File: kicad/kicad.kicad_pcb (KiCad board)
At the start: 4 copper layers, 135 parts, among them Q1 PMF170XP,115, Q2 FS8205A_C2830320, SW1 TS-1088-AR02016, U1 74AHC1G14GW,125, U2 E73-2G4M08S1C, U3 BL8573CS8TR, U4 DW01A, U5 S2B-PH-K-S(LF)(SN), U6 LP5024RSMR, U7 SN74HCS74BQAR, X3 FC-13532.768KHZ9PF20PPM

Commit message: psb outline
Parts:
- removed hex_outline (x36): , clipboard:b9cf7df6-7b49-4194-bf11-16aaca528749
- added hex_edge: , clipboard:b9cf7df6-7b49-4194-bf11-16aaca528749, F.Cu at (104.2, 49.4)
- added hex_edge: , clipboard:b9cf7df6-7b49-4194-bf11-16aaca528749, F.Cu at (215.9, 92.4)
- added hex_edge: , clipboard:b9cf7df6-7b49-4194-bf11-16aaca528749, F.Cu at (215.9, 70.9)
- added hex_edge: , clipboard:b9cf7df6-7b49-4194-bf11-16aaca528749, F.Cu at (178.6, 71.0)
- added hex_edge: , clipboard:b9cf7df6-7b49-4194-bf11-16aaca528749, F.Cu at (215.9, 49.4)
- added hex_edge: , clipboard:b9cf7df6-7b49-4194-bf11-16aaca528749, F.Cu at (104.2, 70.9)
- added hex_edge: , clipboard:b9cf7df6-7b49-4194-bf11-16aaca528749, F.Cu at (197.2, 38.7)
- added hex_edge: , clipboard:b9cf7df6-7b49-4194-bf11-16aaca528749, F.Cu at (122.9, 38.7)
- added hex_edge: , clipboard:b9cf7df6-7b49-4194-bf11-16aaca528749, F.Cu at (122.8, 103.2)
- added hex_edge: , hexcaps:PG1350_hotswap, B.Cu at (160.0, 103.2)
- added hex_edge: , clipboard:b9cf7df6-7b49-4194-bf11-16aaca528749, F.Cu at (141.4, 49.4)
- added hex_edge: , clipboard:b9cf7df6-7b49-4194-bf11-16aaca528749, F.Cu at (178.6, 27.9)
- added hex_edge: , clipboard:b9cf7df6-7b49-4194-bf11-16aaca528749, F.Cu at (160.0, 38.7)
- added hex_edge: , clipboard:b9cf7df6-7b49-4194-bf11-16aaca528749, F.Cu at (104.2, 113.9)
- added hex_edge: , clipboard:b9cf7df6-7b49-4194-bf11-16aaca528749, F.Cu at (160.1, 81.7)
- added hex_edge: , clipboard:b9cf7df6-7b49-4194-bf11-16aaca528749, F.Cu at (197.2, 81.7)
- added hex_edge: , clipboard:b9cf7df6-7b49-4194-bf11-16aaca528749, F.Cu at (104.1, 92.4)
- added hex_edge: , clipboard:b9cf7df6-7b49-4194-bf11-16aaca528749, F.Cu at (141.4, 113.9)
- added key_template (x2): , hexcaps:PG1350_hotswap, B.Cu at (104.2, 92.4)
- added key_template: , hexcaps:PG1350_hotswap, B.Cu at (122.8, 81.7)
- added key_template (x2): , hexcaps:PG1350_hotswap, B.Cu at (104.2, 70.9)
- added key_template: , hexcaps:PG1350_hotswap, B.Cu at (270.7, 45.8)
- Battery?, Q2, R10, R8, R9, U3, U4, U5: moved to B.Cu
- moved C25 38.0 mm to (124.9, 84.2)
- moved R11 38.0 mm to (124.9, 82.9)
- moved R12 38.0 mm to (124.9, 79.2)
- moved R13 38.0 mm to (124.9, 80.4)
- moved R14 38.0 mm to (124.9, 81.7)
- moved U6 38.0 mm to (129.1, 81.1)
- moved C26 38.0 mm to (124.8, 77.8)
- moved U5 35.9 mm to (113.3, 39.7), turned to 0 degrees
- moved U4 34.1 mm to (127.2, 45.3)
- moved Q2 34.0 mm to (127.2, 41.0)
- moved D2 31.5 mm to (100.1, 63.3), turned to 0 degrees
- moved D1 30.4 mm to (102.2, 63.3), turned to 180 degrees
- moved R4 29.9 mm to (100.1, 64.5), turned to 0 degrees
- moved D3 28.8 mm to (102.2, 64.5), turned to 180 degrees
- moved C3 28.3 mm to (100.2, 65.8), turned to 180 degrees
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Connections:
- U6 pad 1: /LED20 -> /LED16
- U6 pad 10: /LED7 -> unconnected-(U6-OUT9-Pad10)
- U6 pad 11: /LED6 -> /LED2
- U6 pad 12: /LED10 -> /LED6
- U6 pad 13: /LED11 -> /LED10
- U6 pad 14: /LED15 -> /LED14
- U6 pad 15: /LED14 -> unconnected-(U6-OUT14-Pad15)
- U6 pad 16: /LED18 -> unconnected-(U6-OUT15-Pad16)
- U6 pad 17: /LED19 -> /LED18
- U6 pad 18: /LED8 -> /LED1
- U6 pad 19: /LED12 -> /LED5
- U6 pad 2: /LED4 -> /LED12
- U6 pad 20: /LED16 -> /LED9
- U6 pad 21: unconnected-(U6-OUT20-Pad21) -> /LED13
- U6 pad 22: unconnected-(U6-OUT21-Pad22) -> /LED17
- U6 pad 23: unconnected-(U6-OUT22-Pad23) -> /LED4
- U6 pad 24: unconnected-(U6-OUT23-Pad24) -> /LED20
- U6 pad 3: /LED17 -> /LED8
- U6 pad 4: /LED13 -> /LED19
- U6 pad 5: /LED9 -> /LED15
- U6 pad 6: /LED5 -> /LED11
- U6 pad 7: /LED1 -> /LED7
- U6 pad 8: /LED2 -> /LED3
- U6 pad 9: /LED3 -> unconnected-(U6-OUT8-Pad9)
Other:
- board outline added: 127.3 x 89.6 mm

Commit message: .
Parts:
- removed D1, D2: NSR05F20NXT5G, easyeda2kicad:DSN2_L1.0-W0.6-RD
- added R15: RC0402FR-074M3L, easyeda2kicad:R0402, F.Cu at (84.2, 65.0)
- added R16: RC0402FR-071ML, easyeda2kicad:R0402, F.Cu at (84.2, 67.1)
- U1: value 74AHC1G14GW,125 -> TLV7031QDCKRQ1; footprint easyeda2kicad:SOT-353_L2.1-W1.3-P0.65-LS2.3-BR -> easyeda2kicad:SC-70-5_L2.0-W1.3-P0.65-LS2.1-BR
- moved R1 18.9 mm to (84.2, 60.7)
- moved D3 18.6 mm to (84.2, 69.2), turned to 0 degrees
- moved Q1 16.3 mm to (87.5, 65.2), turned to 0 degrees
- moved R4 16.0 mm to (84.2, 62.8)
- moved U1 14.4 mm to (87.7, 68.5), turned to 0 degrees
- moved U7 13.0 mm to (88.4, 61.5), turned to 0 degrees
- moved C3 9.37 mm to (90.9, 64.6), turned to 0 degrees
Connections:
- C3 pad 1: Net-(U1-A) -> Net-(U1-IN+)
- D3 pad 1: Net-(D1-Pad1) -> /PWR_BTN
- D3 pad 2: Net-(U1-A) -> Net-(U1-IN+)
- R1 pad 1: Net-(D1-Pad1) -> /PWR_BTN
- R4 pad 1: Net-(D2-Pad1) -> /PWR_BTN
- R4 pad 2: Net-(U1-A) -> Net-(U1-IN+)
- U1 pad 1: unconnected-(U1-NC-Pad1) -> Net-(U1-OUT)
- U1 pad 2: Net-(U1-A) -> GND
- U1 pad 3: GND -> Net-(U1-IN+)
- U1 pad 4: Net-(U1-Y) -> Net-(U1-IN-)
- U1 pad 5: /BAT+ -> /PWR_BTN
- U7 pad 3: Net-(U1-Y) -> Net-(U1-OUT)

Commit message: ..
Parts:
- added component_safe_space: , hexcaps:PG1350_hotswap, B.Cu at (104.1, 92.4)
- added component_safe_space: , hexcaps:PG1350_hotswap, B.Cu at (104.2, 70.9)
- added component_safe_space: , hexcaps:PG1350_hotswap, B.Cu at (122.8, 81.7)
- moved C3 12.2 mm to (102.3, 68.9)
- moved D3 12.2 mm to (95.7, 73.6)
- moved Q1 12.2 mm to (99.0, 69.5)
- moved R16 12.2 mm to (95.6, 71.4)
- moved R4 12.2 mm to (95.6, 67.1)
- moved R1 12.2 mm to (95.6, 65.0)
- moved U7 12.2 mm to (99.9, 65.8)
- moved R15 12.2 mm to (95.6, 69.3)
- moved U1 12.2 mm to (99.2, 72.8)
- moved C25 2.72 mm to (122.2, 84.9)
- moved C26 2.72 mm to (122.2, 78.6)
- moved R11 2.72 mm to (122.2, 83.7)
- moved R12 2.72 mm to (122.2, 79.9)
- moved R13 2.72 mm to (122.2, 81.2)
- moved R14 2.72 mm to (122.2, 82.4)
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- renumbered key_template to component_case_outline

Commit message: ...
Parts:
- added C10: GRM033C71C104KE14D, easyeda2kicad:C0201, F.Cu at (98.3, 29.6)
- added C11: GRM033C71C104KE14D, easyeda2kicad:C0201, F.Cu at (99.3, 31.2)
- added C12: GRM033C71C104KE14D, easyeda2kicad:C0201, F.Cu at (100.3, 32.9)
- added C13: GRM033C71C104KE14D, easyeda2kicad:C0201, F.Cu at (98.6, 24.9)
- added C14: GRM033C71C104KE14D, easyeda2kicad:C0201, F.Cu at (99.6, 26.6)
- added C15: GRM033C71C104KE14D, easyeda2kicad:C0201, F.Cu at (100.5, 28.3)
- added C16: GRM033C71C104KE14D, easyeda2kicad:C0201, F.Cu at (101.5, 30.0)
- added C17: GRM033C71C104KE14D, easyeda2kicad:C0201, F.Cu at (102.5, 31.6)
- added C18: GRM033C71C104KE14D, easyeda2kicad:C0201, F.Cu at (100.8, 23.7)
- added C19: GRM033C71C104KE14D, easyeda2kicad:C0201, F.Cu at (101.8, 25.4)
- added C20: GRM033C71C104KE14D, easyeda2kicad:C0201, F.Cu at (102.7, 27.0)
- added C21: GRM033C71C104KE14D, easyeda2kicad:C0201, F.Cu at (103.7, 28.7)
- added C22: GRM033C71C104KE14D, easyeda2kicad:C0201, F.Cu at (104.7, 30.4)
- added C23: GRM033C71C104KE14D, easyeda2kicad:C0201, F.Cu at (103.0, 22.4)
- added C24: GRM033C71C104KE14D, easyeda2kicad:C0201, F.Cu at (104.0, 24.1)
- added C25: GRM033C71C104KE14D, easyeda2kicad:C0201, F.Cu at (104.9, 25.8)
- added C26: GRM033C71C104KE14D, easyeda2kicad:C0201, F.Cu at (105.9, 27.4)
- added C27: GRM033C71C104KE14D, easyeda2kicad:C0201, F.Cu at (106.8, 29.1)
- added C8: GRM033C71C104KE14D, easyeda2kicad:C0201, F.Cu at (96.4, 26.2)
- added C9: GRM033C71C104KE14D, easyeda2kicad:C0201, F.Cu at (97.4, 27.9)
- turned R8 to 180 degrees
- renumbered C3 to C1, C11 to C2, C27 to C3, C28 to C4, C29 to C5, C25 to C6, C26 to C7, D3 to D1, D13 to D10, D17 to D11, D21 to D12, D15 to D13, D6 to D14, D10 to D15, D14 to D16, D18 to D17, D22 to D18, D11 to D19, D4 to D2, D19 to D20, D8 to D3, D12 to D4, D16 to D5, D20 to D6, D5 to D8, LED17 to LED10, LED4 to LED11, LED14 to LED12, LED11 to LED13, LED8 to LED14, LED18 to LED15, LED15 to LED16, LED12 to LED17, LED19 to LED18, LED16 to LED19, LED5 to LED2, LED2 to LED3, LED9 to LED4, LED6 to LED5, LED3 to LED6, LED13 to LED7, LED10 to LED8, LED7 to LED9, R4 to R1, R5 to R10, R2 to R11, R3 to R12, R11 to R13, R12 to R14, R13 to R15, R14 to R16, R6 to R2, R8 to R3, R9 to R4, R10 to R5, R1 to R6, R15 to R8, R16 to R9, S14 to S11, S18 to S12, S12 to S13, S3 to S14, S7 to S15, S11 to S16, S15 to S17, S19 to S18, S8 to S19, S5 to S2, S16 to S20, S9 to S3, S13 to S4, S17 to S5, S4 to S6, S20 to S7, S2 to S8, S6 to S9, U4 to U1, U3 to U2, U1 to U3, U7 to U4, U2 to U6, U6 to U7, X3 to X1

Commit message: ... started doing wiring
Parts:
- C1, C10, D1, Q1: moved to B.Cu
- C11: renamed from C20; moved to B.Cu
- C12: renamed from C11; moved to B.Cu
- C13: renamed from C21; moved to B.Cu
- C14: renamed from C12; moved to B.Cu
- C15: renamed from C22; moved to B.Cu
- C16: renamed from C13; moved to B.Cu
- C17: renamed from C23; moved to B.Cu
- C18: renamed from C14; moved to B.Cu
- C19: renamed from C24; moved to B.Cu
- C20: renamed from C15; moved to B.Cu
- C21: renamed from C25; moved to B.Cu
- C22: renamed from C16; moved to B.Cu
- C23: renamed from C26; moved to B.Cu
- C24: renamed from C17; moved to B.Cu
- C25: renamed from C27; moved to B.Cu
- C6: renamed from C8; moved to B.Cu
- C7: renamed from C18; moved to B.Cu
- C8: renamed from C9; moved to B.Cu
- C9: renamed from C19; moved to B.Cu
- R1: renamed from R6; moved to B.Cu
- R2: renamed from R1; moved to B.Cu
- R3: renamed from R8; moved to B.Cu
- R6: renamed from R9; moved to B.Cu
- U1: renamed from U3; moved to B.Cu
- U3: renamed from U4; moved to B.Cu
- moved C8 133.1 mm to (216.9, 86.4)
- moved C7 123.2 mm to (216.9, 64.9)
- moved C6 121.7 mm to (216.9, 43.4)
- moved C12 108.5 mm to (198.3, 75.6)
- moved C10 100.0 mm to (198.3, 32.6)
- moved C11 99.3 mm to (198.3, 54.1)
- moved C16 90.3 mm to (179.7, 64.9)
- moved C13 88.1 mm to (142.4, 107.9), turned to -150 degrees
- moved C21 82.1 mm to (105.2, 107.9), turned to -150 degrees
- moved C14 80.1 mm to (179.7, 21.9)
- moved C17 77.5 mm to (123.8, 97.1), turned to -150 degrees
- moved C20 76.8 mm to (161.0, 75.6)
- moved C15 76.1 mm to (179.7, 43.4)
- moved C24 67.8 mm to (142.4, 86.4)
- moved C19 64.5 mm to (161.0, 54.1)
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- renumbered C4 to C2, C6 to C26, C7 to C27, C5 to C3, C2 to C4, C3 to C5, D16 to D10, D5 to D11, D11 to D12, D17 to D13, D6 to D14, D12 to D15, D18 to D16, D7 to D17, D13 to D18, D8 to D3, D14 to D4, D3 to D5, D9 to D6, D15 to D7, D4 to D8, D10 to D9, LED8 to LED10, LED13 to LED11, LED17 to LED12, LED7 to LED13, LED12 to LED14, LED16 to LED15, LED19 to LED16, LED10 to LED17, LED15 to LED18, LED18 to LED19, LED3 to LED2, LED6 to LED3, LED11 to LED4, LED2 to LED5, LED5 to LED6, LED9 to LED7, LED14 to LED8, LED4 to LED9, R3 to R10, R4 to R11, R5 to R12, R11 to R4, R12 to R5, R10 to R7, R2 to R8, R7 to R9, S4 to S10, S17 to S12, S5 to S13, S12 to S14, S18 to S15, S6 to S16, S13 to S17, S19 to S18, S20 to S19, S8 to S2, S7 to S20, S14 to S3, S2 to S4, S9 to S5, S15 to S6, S3 to S7, S10 to S8, S16 to S9, U6 to U2, U2 to U4, U1 to U5, U5 to U6
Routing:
- net /PWR_BTN: track 0.00 -> 31.0 mm
- net GND: track 0.00 -> 26.2 mm, vias 0 -> 1
- net /PMOS_gate: track 0.00 -> 13.3 mm
- net /BAT+: track 0.00 -> 8.96 mm, vias 0 -> 2
- net Net-(U1-IN+): track 0.00 -> 4.20 mm
- net Net-(U1-IN-): track 0.00 -> 2.86 mm
- net Net-(F1-Pad1): track 0.00 -> 2.74 mm, vias 0 -> 2
- net Net-(U1-OUT): track 0.00 -> 1.98 mm
- net /PWR: track 0.00 -> 0.88 mm, vias 0 -> 1

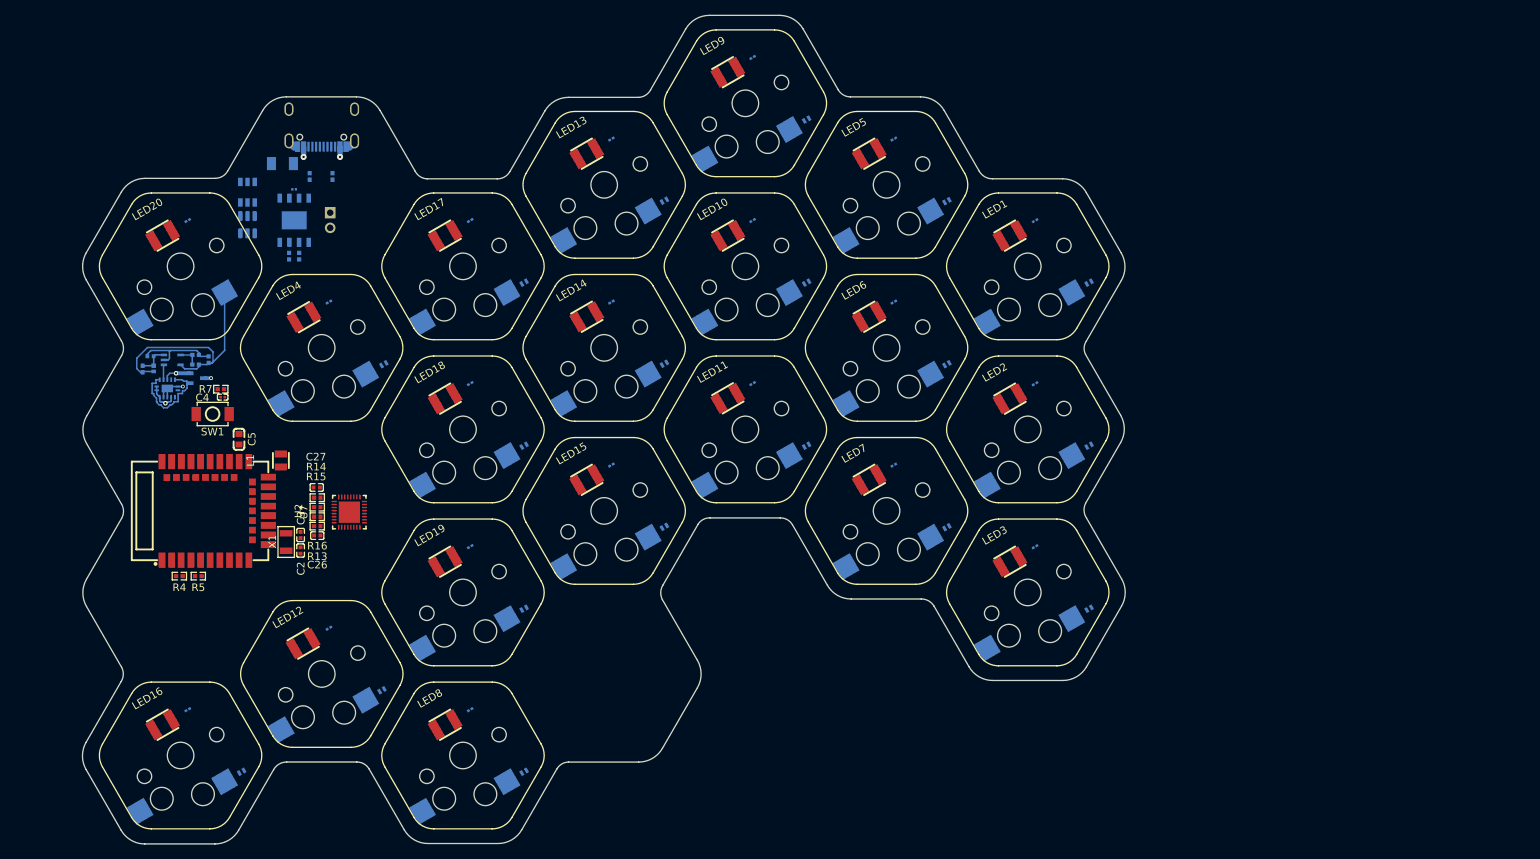
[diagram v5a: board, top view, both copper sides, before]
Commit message: finished part placement and wiring. TODO: wire swd pins. mirror the board for left side.
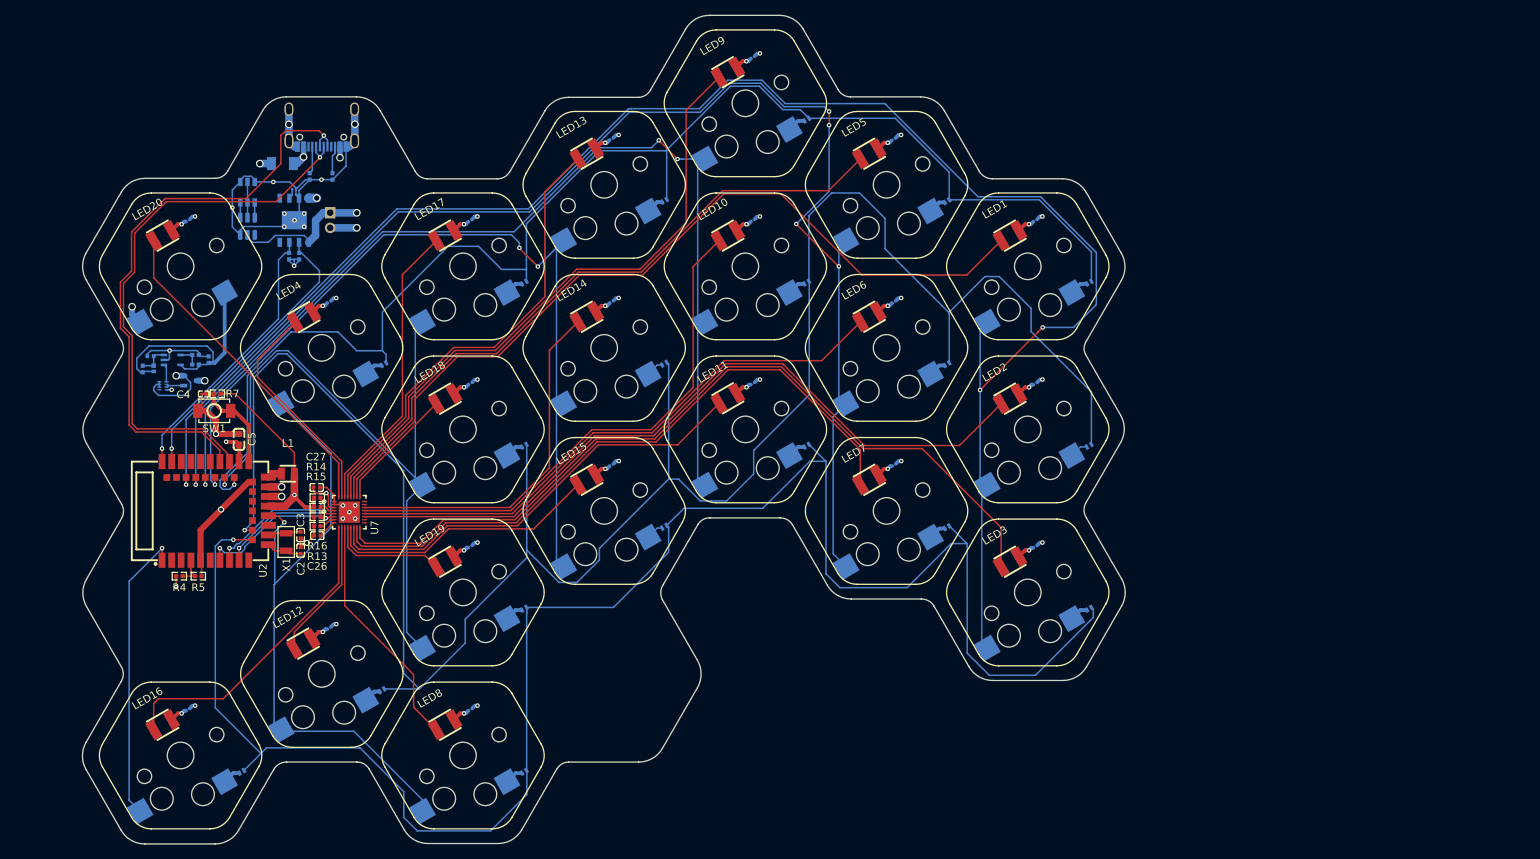
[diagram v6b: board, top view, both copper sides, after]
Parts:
- U3: value SN74HCS74BQAR -> SN74LVC1G74DQER; footprint easyeda2kicad:DQFN-14_L3.0-W2.5-P0.50-BL-EP -> easyeda2kicad:X2SON-8_L1.4-W1.0-P0.35-BL
- moved Battery? 2.81 mm to (129.9, 75.8)
- moved C4 2.54 mm to (107.3, 66.2)
- moved L1 1.97 mm to (118.4, 76.7), turned to 0 degrees
- moved Q1 0.87 mm to (105.5, 64.5)
- moved R7 0.76 mm to (109.1, 66.2), turned to 180 degrees
- moved U3 0.67 mm to (101.9, 65.2), turned to -90 degrees
- moved SW1 0.47 mm to (108.7, 68.5)
- moved U5 0.21 mm to (113.0, 44.1)
- turned C13 to 30 degrees
- turned C17 to 30 degrees
- turned C21 to 30 degrees
- turned C25 to 30 degrees
- turned C9 to 30 degrees
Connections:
- U2 pad 41: /CHRG -> /STDBY
- U2 pad 43: /STDBY -> /CHRG
- U3 pad 1: /BAT+ -> Net-(U1-OUT)
- U3 pad 3: Net-(U1-OUT) -> /PMOS_gate
- U3 pad 4: /BAT+ -> GND
- U3 pad 6: /PMOS_gate -> /BAT+
- U3 pad 7: GND -> /BAT+
- U3 pad 8: unconnected-(U3-~{2Q}-Pad8) -> /BAT+
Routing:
- net /ROW2: track 0.00 -> 286.0 mm, vias 0 -> 1
- net /ROW3: track 0.00 -> 236.7 mm, vias 0 -> 1
- net /COL1: track 0.00 -> 230.1 mm, vias 0 -> 3
- net /COL2: track 0.00 -> 183.2 mm, vias 0 -> 5
- net /ROW1: track 0.00 -> 182.5 mm, vias 0 -> 1
- net /COL3: track 0.00 -> 137.1 mm, vias 0 -> 3
- net /COL4: track 0.00 -> 115.5 mm, vias 0 -> 3
- net /LED1: track 0.00 -> 110.9 mm
- net /LED3: track 0.00 -> 109.9 mm
- net GND: track 26.2 -> 133.4 mm, vias 1 -> 42
- net /LED2: track 0.00 -> 99.0 mm
- net /COL5: track 0.00 -> 93.6 mm, vias 0 -> 1
- net /LED5: track 0.00 -> 88.4 mm
- net /LED7: track 0.00 -> 87.2 mm
- net /COL6: track 0.00 -> 84.3 mm, vias 0 -> 1
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- added copper zone on In2.Cu, net /PWR
- added copper zone on In1.Cu, net GND

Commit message: .
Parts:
- added H1: HC-PM254-8.5H-1X3PW, easyeda2kicad:HDR-TH_3P-P2.54_HC-PM254-8.5H-1X3PW, B.Cu at (99.5, 98.9)
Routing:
- net /SWDIO: track 0.00 -> 30.6 mm, vias 0 -> 1
- net /SWBCLK: track 0.00 -> 27.5 mm, vias 0 -> 1
- net GND: track 133.4 -> 143.4 mm

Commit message: added art... and some other stuff
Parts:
- removed U5: DW01A, Package_TO_SOT_SMD:SOT-23-6
- removed the hex_edge at (160.0, 103.2)
- added G**: LOGO, images:handy, F.Cu at (127.2, 36.1)
- added G***: LOGO, images:monster, B.Cu at (154.2, -8.70)
- added G***: LOGO, images:monster, B.Cu at (164.6, 79.3)
- added S12: Choc HEX, hexcaps:PG1350_hotswap, B.Cu at (160.1, 103.2)
- added U8: DW01A_C42380662, easyeda2kicad:SOT-23-6_L2.9-W1.6-P0.95-LS2.9-BL, B.Cu at (113.0, 44.1)
- moved LED4 77.6 mm to (195.0, 34.5)
- moved LED8 74.5 mm to (176.4, 45.4)
- moved LED17 57.0 mm to (120.4, 99.2)
- moved LED7 56.9 mm to (176.4, 23.8)
- moved LED16 56.9 mm to (120.5, 56.1)
- moved LED12 43.2 mm to (157.8, 77.5)
- moved LED19 43.0 mm to (101.9, 109.8)
- moved LED18 43.0 mm to (139.1, 109.8)
- moved LED9 43.0 mm to (176.4, 66.8)
- moved key_template 25.6 mm to (270.5, 24.2)
- moved LED13 21.6 mm to (139.1, 45.4)
- moved LED14 21.6 mm to (139.1, 66.8)
- moved LED15 21.6 mm to (139.1, 88.3)
- moved LED10 21.5 mm to (157.8, 34.5)
- moved LED5 21.5 mm to (195.0, 56.0)
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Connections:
- U7 pad 1: /LED16 -> /LED19
- U7 pad 12: /LED6 -> /LED5
- U7 pad 13: /LED10 -> /LED8
- U7 pad 14: /LED14 -> /LED11
- U7 pad 17: /LED18 -> /LED14
- U7 pad 19: /LED5 -> /LED4
- U7 pad 2: /LED12 -> /LED17
- U7 pad 20: /LED9 -> /LED7
- U7 pad 21: /LED13 -> /LED10
- U7 pad 22: /LED17 -> /LED13
- U7 pad 23: /LED4 -> /LED16
- U7 pad 3: /LED8 -> /LED18
- U7 pad 4: /LED19 -> /LED15
- U7 pad 5: /LED15 -> /LED12
- U7 pad 6: /LED11 -> /LED9
- U7 pad 7: /LED7 -> /LED6
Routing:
- net /LED4: track 29.7 -> 88.4 mm
- net /LED8: track 31.7 -> 70.8 mm
- net /LED14: track 47.4 -> 16.5 mm
- net /LED19: track 15.4 -> 41.8 mm
- net /LED9: track 83.4 -> 58.6 mm
- net /LED13: track 60.3 -> 38.8 mm
- net /LED15: track 36.4 -> 15.4 mm
- net /LED17: track 38.8 -> 18.6 mm
- net /LED12: track 18.6 -> 36.4 mm
- net /LED18: track 16.5 -> 31.7 mm
- net /LED5: track 88.4 -> 75.9 mm
- net /LED16: track 41.8 -> 29.7 mm
- net /LED6: track 75.9 -> 87.2 mm
- net /LED11: track 58.6 -> 47.4 mm
- net /LED10: track 70.8 -> 60.3 mm
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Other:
- outline, holes or cut-outs redrawn
